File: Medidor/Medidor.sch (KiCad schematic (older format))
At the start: 28 parts, among them X1 32MHz

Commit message: Corrigindo DC-DC
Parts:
- added C12: 0.33uF, symbol Device:C_Small
- added C13: 0.1uF, symbol Device:C_Small
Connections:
- wire segments 121 -> 127
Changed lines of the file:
@@
 L power:+3V3 #PWR0131
 U 1 1 5D4BE21E
-P 2600 6300
-F 0 "#PWR0131" H 2600 6150 50  0001 C CNN
-F 1 "+3V3" H 2615 6473 50  0000 C CNN
-F 2 "" H 2600 6300 50  0001 C CNN
-F 3 "" H 2600 6300 50  0001 C CNN
-	1    2600 6300
+P 2600 5950
+F 0 "#PWR0131" H 2600 5800 50  0001 C CNN
+F 1 "+3V3" H 2615 6123 50  0000 C CNN
+F 2 "" H 2600 5950 50  0001 C CNN
+F 3 "" H 2600 5950 50  0001 C CNN
+	1    2600 5950
 	1    0    0    -1
 $EndComp
@@
 	2450 6500 2600 6500
 Wire Wire Line
-	2600 6500 2600 6300
+	2600 6500 2600 6250
 $Comp
 L power:+5V #PWR0132
@@
 L power:+5V #PWR0133
 U 1 1 5D4E00B3
-P 1650 6300
-F 0 "#PWR0133" H 1650 6150 50  0001 C CNN
-F 1 "+5V" H 1665 6473 50  0000 C CNN
-F 2 "" H 1650 6300 50  0001 C CNN
-F 3 "" H 1650 6300 50  0001 C CNN
-	1    1650 6300
+P 1650 5950
+F 0 "#PWR0133" H 1650 5800 50  0001 C CNN
+F 1 "+5V" H 1665 6123 50  0000 C CNN
+F 2 "" H 1650 5950 50  0001 C CNN
+F 3 "" H 1650 5950 50  0001 C CNN
+	1    1650 5950
 	1    0    0    -1
 $EndComp
 Wire Wire Line
 	1800 6500 1650 6500
-Wire Wire Line
-	1650 6500 1650 6300
 $Comp
 L power:Earth #PWR0134
@@
 NoConn ~ 4750 4850
 NoConn ~ 4750 4950
+$Comp
+L Device:C_Small C12
+U 1 1 5D5298BC
+P 1350 6350
+F 0 "C12" H 1200 6300 50  0000 C CNN
+F 1 "0.33uF" H 1200 6450 50  0000 C CNN
+F 2 "" H 1350 6350 50  0001 C CNN
+F 3 "~" H 1350 6350 50  0001 C CNN
+	1    1350 6350
+	-1   0    0    1
+$EndComp
+$Comp
+L Device:C_Small C13
+U 1 1 5D52A5CF
+P 2900 6350
+F 0 "C13" H 2750 6300 50  0000 C CNN
+F 1 "0.1uF" H 2750 6450 50  0000 C CNN
+F 2 "" H 2900 6350 50  0001 C CNN
+F 3 "~" H 2900 6350 50  0001 C CNN
+	1    2900 6350
+	-1   0    0    1
+$EndComp
+Wire Wire Line
+	1650 6500 1650 6250
+Wire Wire Line
+	1350 6250 1650 6250
+Connection ~ 1650 6250
+Wire Wire Line
+	1650 6250 1650 5950
+$Comp
+L power:Earth #PWR0138
+U 1 1 5D53C83C
+P 1350 6750
+F 0 "#PWR0138" H 1350 6500 50  0001 C CNN
+F 1 "Earth" H 1350 6600 50  0001 C CNN
+F 2 "" H 1350 6750 50  0001 C CNN
+F 3 "~" H 1350 6750 50  0001 C CNN
+	1    1350 6750
+	1    0    0    -1
+$EndComp
+Wire Wire Line
+	1350 6750 1350 6450
+Wire Wire Line
+	2900 6250 2600 6250
+Connection ~ 2600 6250
+Wire Wire Line
+	2600 6250 2600 5950
+$Comp
+L power:Earth #PWR0139
+U 1 1 5D54C6B0
+P 2900 6750
+F 0 "#PWR0139" H 2900 6500 50  0001 C CNN
+F 1 "Earth" H 2900 6600 50  0001 C CNN
+F 2 "" H 2900 6750 50  0001 C CNN
+F 3 "~" H 2900 6750 50  0001 C CNN
+	1    2900 6750
+	1    0    0    -1
+$EndComp
+Wire Wire Line
+	2900 6750 2900 6450
 $EndSCHEMATC

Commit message: Esquemático mais completo.
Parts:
- removed C12: 0.33uF, symbol Device:C_Small
- removed C5, C6: 10uF, symbol Device:C_Small
- removed Entrada1: terminal, symbol medidor:terminal
- removed Fil1: 2450FM07A0029T, symbol medidor:2450FM07A0029T
- removed INA1: INA219, symbol medidor:INA219
- removed L3: 10nH, symbol Device:L_Small
- removed dc1: DC-DC, symbol medidor:DC-DC
- added C12: 0.1u, symbol Device:CP
- added C14, C15: 0.1uF, symbol Device:C_Small
- added C16: 0.33u, symbol Device:CP
- added Fil1: 2450FM07A0029T-medidor, symbol Medidor-rescue:2450FM07A0029T-medidor
- added J1: TC2030-CTX-TAG_CONECT, symbol Medidor-rescue:TC2030-CTX-TAG_CONECT
- added R10, R11, R12, R9: 1K, symbol Device:R_Small_US
- added R4, R5, R7: 1k, symbol Device:R_Small_US
- added R6, R8: NC, symbol Device:R_Small_US
- added SW1: Rotary_Encoder_Switch, symbol Device:Rotary_Encoder_Switch
- added SW2: SW_DPST_x2, symbol Switch:SW_DPST_x2
- added TER1: terminal-medidor, symbol Medidor-rescue:terminal-medidor
- added U1: INA219-INA, SOT23-8, symbol Medidor-rescue:INA219-INA
- added dc1: DC-DC, symbol Medidor-rescue:DC-DC-medidor
- C13: value 0.1uF -> NC
- R2, R3: value 10k -> 1k
- renumbered R4 to R13
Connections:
- net labels added: A0, A1, AIN0, AIN1, SCL, SDA, SWDCLK, SWDIO, nRESET
- net labels removed: DysplaySCL, DysplaySDA, INASCL, INASDA
- wire segments 127 -> 175
- no-connect marks 34 -> 27
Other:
- note added: "Rotary Code"
- moved on the sheet: ANT1, C11, R1, R2, R3

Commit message: Correção no circuito do encoder
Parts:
- added R13: 1K, symbol Device:R_Small_US
- Display1: symbol medidor:OLED -> Medidor-rescue:OLED-medidor
- MCU1: symbol medidor:nRF52832-QFN4 -> Medidor-rescue:nRF52832-QFN4-medidor
- US1: symbol medidor:USB -> Medidor-rescue:USB-medidor
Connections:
- wire segments 175 -> 178
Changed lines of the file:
@@
 L power:+3V3 #PWR0145
 U 1 1 5D45CE3B
-P 1900 4650
-F 0 "#PWR0145" H 1900 4500 50  0001 C CNN
-F 1 "+3V3" H 1915 4823 50  0000 C CNN
-F 2 "" H 1900 4650 50  0001 C CNN
-F 3 "" H 1900 4650 50  0001 C CNN
-	1    1900 4650
+P 1550 4500
+F 0 "#PWR0145" H 1550 4350 50  0001 C CNN
+F 1 "+3V3" H 1565 4673 50  0000 C CNN
+F 2 "" H 1550 4500 50  0001 C CNN
+F 3 "" H 1550 4500 50  0001 C CNN
+	1    1550 4500
 	1    0    0    -1
 $EndComp
@@
 	1    0    0    -1
 $EndComp
-Wire Wire Line
-	2350 4650 2100 4650
 Wire Wire Line
 	2100 4650 2100 4800
@@
 $EndComp
 $Comp
-L medidor:nRF52832-QFN4 MCU1
+L Medidor-rescue:nRF52832-QFN4-medidor MCU1
 U 1 1 5D5C14BA
 P 5650 4400
@@
 $EndComp
 $Comp
-L medidor:USB US1
+L Medidor-rescue:USB-medidor US1
 U 1 1 5D5EBF95
 P 850 7250
@@
 $EndComp
 $Comp
-L medidor:OLED Display1
+L Medidor-rescue:OLED-medidor Display1
 U 1 1 5D5F6826
 P 1700 3700
@@
 Wire Notes Line
 	4500 600  3000 600
+Wire Wire Line
+	2350 4650 2100 4650
+$Comp
+L Device:R_Small_US R13
+U 1 1 5D352B3E
+P 1700 4650
+F 0 "R13" V 1750 4800 50  0000 C CNN
+F 1 "1K" V 1750 4500 50  0000 C CNN
+F 2 "" H 1700 4650 50  0001 C CNN
+F 3 "~" H 1700 4650 50  0001 C CNN
+	1    1700 4650
+	0    -1   -1   0
+$EndComp
+Wire Wire Line
+	1900 4650 1800 4650
+Wire Wire Line
+	1600 4650 1550 4650
+Wire Wire Line
+	1550 4650 1550 4500
 $EndSCHEMATC

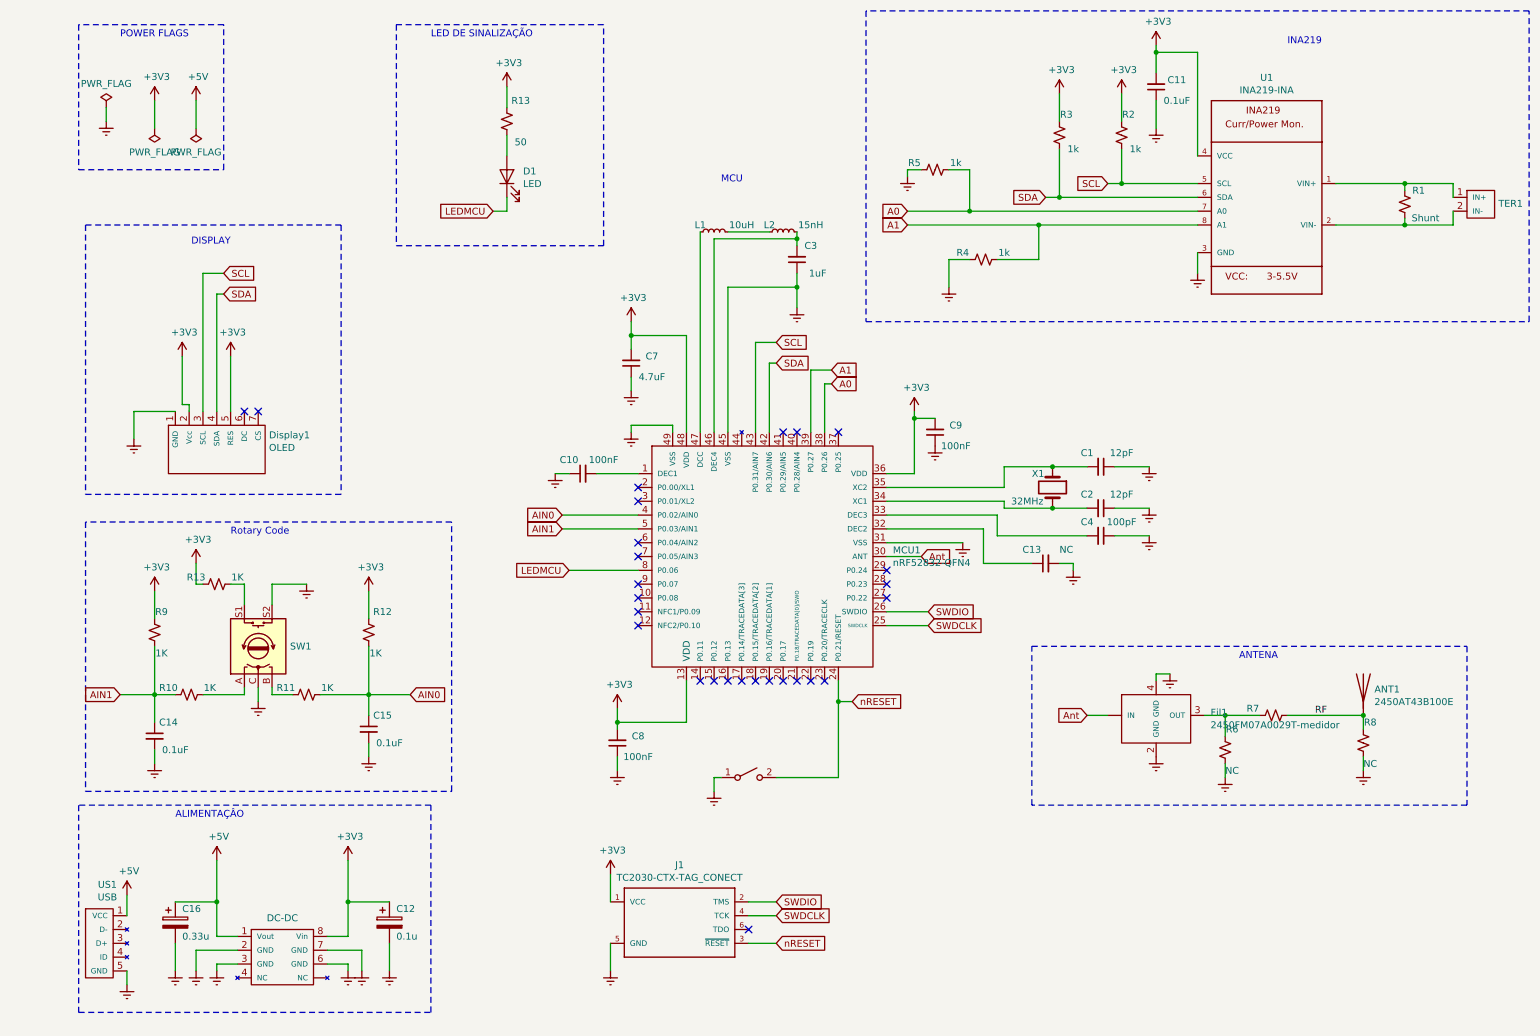
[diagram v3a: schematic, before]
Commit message: Add Uart e filtro no ina.
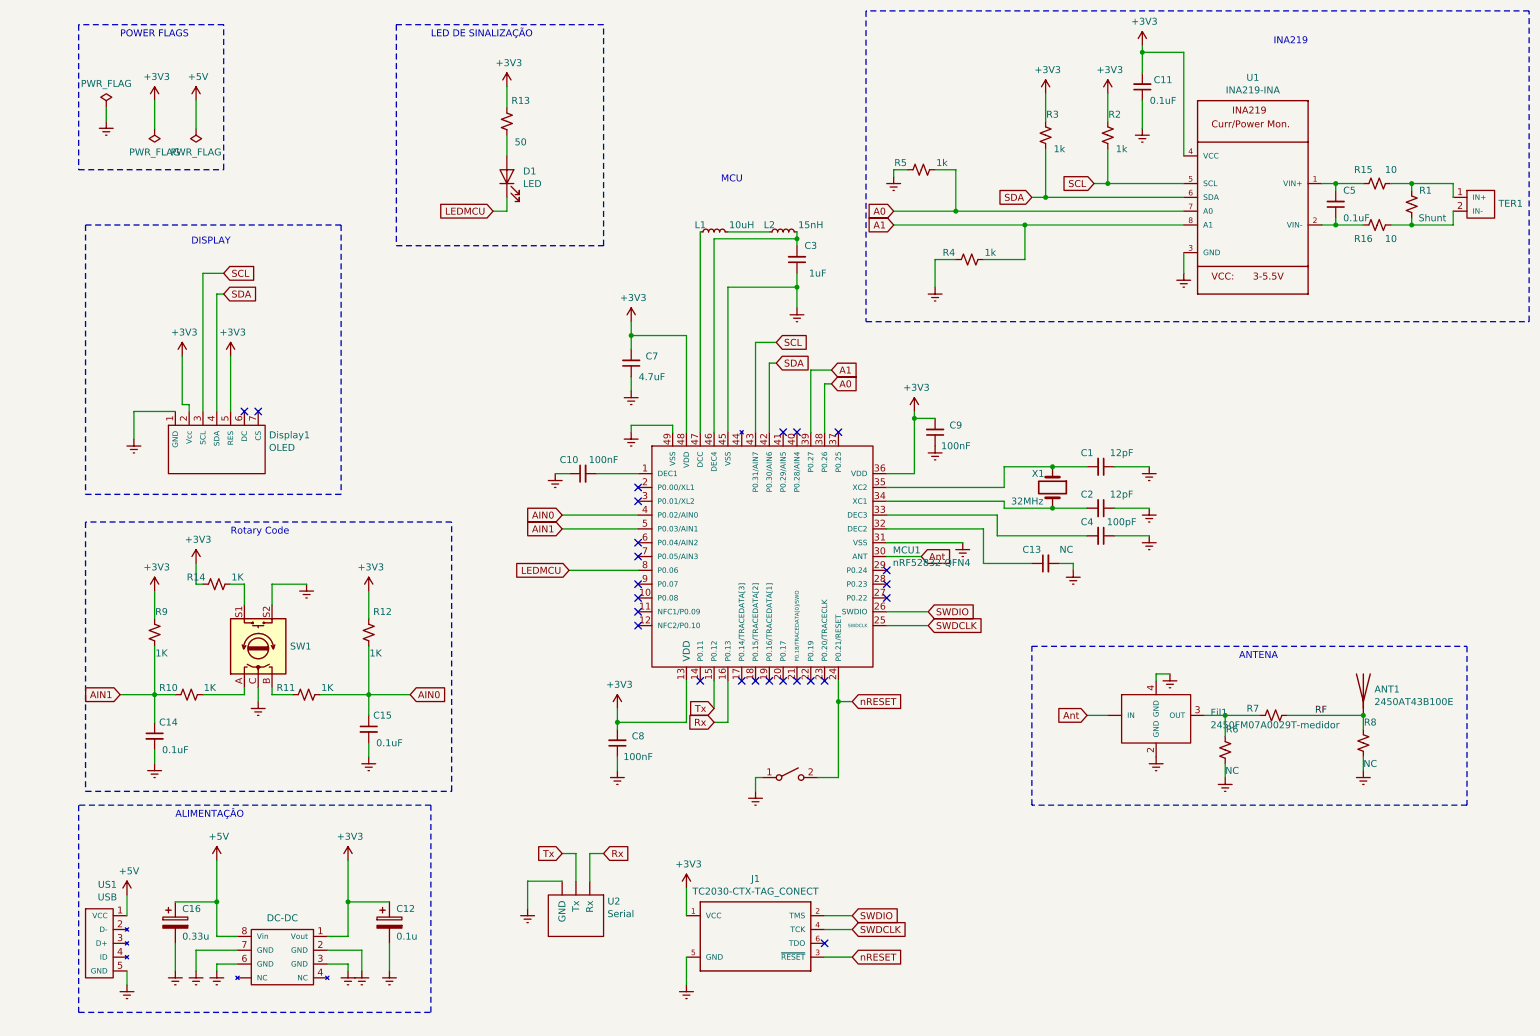
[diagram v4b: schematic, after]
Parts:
- added C5: 0.1uF, symbol Device:C_Small
- added R15, R16: 10, symbol Device:R_Small_US
- added U2: Serial, symbol medidor:Serial
- renumbered R13 to R14
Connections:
- net +3V3: now also dc1.1 (Vout); no longer dc1.8 (Vin)
- net +5V: now also dc1.8 (Vin); no longer dc1.1 (Vout)
- net Earth: now also U2.~ (Tx)
- net at R1.2, TER1.1 (IN+): now also R15.1; no longer U1.1 (VIN+)
- net at R1.1, TER1.2 (IN-): now also R16.1; no longer U1.2 (VIN-)
- net Tx: now reaches MCU1.15 (P0.12)
- net Tx: now also U2.~ (Tx)
- net Rx: now reaches MCU1.16 (P0.13)
- net Rx: now also U2.~ (Tx)
- new net: C5.1, R16.2, U1.2 (VIN-)
- new net: C5.2, R15.2, U1.1 (VIN+)
- no-connect marks 27 -> 25
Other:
- moved on the sheet: C11, J1, R1, R2, R3, R4, R5, U1

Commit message: Minor fix
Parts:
- R10, R11, R12, R14, R9: value 1K -> 10K
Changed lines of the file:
@@
 P 1250 5000
 F 0 "R9" H 1300 5150 50  0000 C CNN
-F 1 "1K" H 1300 4850 50  0000 C CNN
+F 1 "10K" H 1350 4850 50  0000 C CNN
 F 2 "" H 1250 5000 50  0001 C CNN
 F 3 "~" H 1250 5000 50  0001 C CNN
@@
 P 1500 5450
 F 0 "R10" V 1550 5600 50  0000 C CNN
-F 1 "1K" V 1550 5300 50  0000 C CNN
+F 1 "10K" V 1550 5300 50  0000 C CNN
 F 2 "" H 1500 5450 50  0001 C CNN
 F 3 "~" H 1500 5450 50  0001 C CNN
@@
 P 2350 5450
 F 0 "R11" V 2400 5600 50  0000 C CNN
-F 1 "1K" V 2400 5300 50  0000 C CNN
+F 1 "10K" V 2400 5300 50  0000 C CNN
 F 2 "" H 2350 5450 50  0001 C CNN
 F 3 "~" H 2350 5450 50  0001 C CNN
@@
 P 2800 5000
 F 0 "R12" H 2900 5150 50  0000 C CNN
-F 1 "1K" H 2850 4850 50  0000 C CNN
+F 1 "10K" H 2900 4850 50  0000 C CNN
 F 2 "" H 2800 5000 50  0001 C CNN
 F 3 "~" H 2800 5000 50  0001 C CNN
@@
 P 1700 4650
 F 0 "R14" V 1750 4800 50  0000 C CNN
-F 1 "1K" V 1750 4500 50  0000 C CNN
+F 1 "10K" V 1750 4500 50  0000 C CNN
 F 2 "" H 1700 4650 50  0001 C CNN
 F 3 "~" H 1700 4650 50  0001 C CNN
